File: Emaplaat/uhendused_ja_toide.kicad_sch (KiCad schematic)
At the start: 35 parts, among them IC4 TPS54429PWPR, IC5 FT232RNL-TUBE, J1 694108301002, J2 USB4216-03-A

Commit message: natuke parandusi
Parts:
- D7, D8, D9: Voltage (none) -> 3.3
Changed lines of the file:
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@@
 			)
 		)
+		(property "Voltage" "3.3"
+			(at 90.17 135.636 90)
+			(effects
+				(font
+					(size 1.27 1.27)
+				)
+			)
+		)
 		(pin "2"
 		)
@@
 	)
 	(symbol
-		(lib_name "CPDH3V3UP-HF_4")
-		(lib_id "CPDH3V3UP-HF:CPDH3V3UP-HF")
-		(at 91.44 115.57 270)
-		(unit 1)
-		(exclude_from_sim no)
-		(in_bom yes)
-		(on_board yes)
-		(dnp no)
-		(property "Reference" "D9"
-			(at 93.472 123.19 90)
-			(effects
-				(font
-					(size 1.27 1.27)
-				)
-				(justify left)
-			)
-		)
-		(property "Value" "CPDH3V3UP-HF"
-			(at 80.772 137.922 90)
-			(effects
-				(font
-					(size 1.27 1.27)
-				)
-				(justify left)
-			)
-		)
-		(property "Footprint" "Diode_SMD:D_SOD-523"
-			(at -2.21 125.73 0)
-			(effects
-				(font
-					(size 1.27 1.27)
-				)
-				(justify left bottom)
-				(hide yes)
-			)
-		)
-		(property "Datasheet" "https://datasheet.datasheetarchive.com/originals/distributors/Datasheets-DGA26/1842371.pdf"
-			(at -102.21 125.73 0)
-			(effects
-				(font
-					(size 1.27 1.27)
-				)
-				(justify left bottom)
-				(hide yes)
-			)
-		)
-		(property "Description" "ESD Suppressors / TVS Diodes 5.5V, 15Kv"
-			(at 105.156 115.316 0)
-			(effects
-				(font
-					(size 1.27 1.27)
-				)
-				(hide yes)
-			)
-		)
-		(property "Height" "0.77"
-			(at -302.21 125.73 0)
-			(effects
-				(font
-					(size 1.27 1.27)
-				)
-				(justify left bottom)
-				(hide yes)
-			)
-		)
-		(property "Mouser Part Number" "750-CPDH3V3UP-HF"
-			(at -402.21 125.73 0)
-			(effects
-				(font
-					(size 1.27 1.27)
-				)
-				(justify left bottom)
-				(hide yes)
-			)
-		)
-		(property "Mouser Price/Stock" "https://www.mouser.co.uk/ProductDetail/Comchip-Technology/CPDH3V3UP-HF?qs=XEIV%2Fho1H6em2DT135enQw%3D%3D"
-			(at -502.21 125.73 0)
-			(effects
-				(font
-					(size 1.27 1.27)
-				)
-				(justify left bottom)
-				(hide yes)
-			)
-		)
-		(property "Manufacturer_Name" "Comchip Technology"
-			(at -602.21 125.73 0)
-			(effects
-				(font
-					(size 1.27 1.27)
-				)
-				(justify left bottom)
-				(hide yes)
-			)
-		)
-		(property "Manufacturer_Part_Number" "CPDH3V3UP-HF"
-			(at -702.21 125.73 0)
-			(effects
-				(font
-					(size 1.27 1.27)
-				)
-				(justify left bottom)
-				(hide yes)
-			)
-		)
-		(pin "1"
-		)
-		(pin "2"
-		)
-		(instances
-			(project "Emaplaat"
-				(path "/489224c0-ace1-4530-aa61-a5d03adf1434/902edf26-f9ad-46ee-8658-d4b7491aa9c7"
-					(reference "D9")
-					(unit 1)
-				)
-			)
-		)
-	)
-	(symbol
 		(lib_id "Device:R")
 		(at 66.04 127 0)
@@
 	)
 	(symbol
+		(lib_name "CPDH3V3UP-HF_2")
+		(lib_id "CPDH3V3UP-HF:CPDH3V3UP-HF")
+		(at 91.44 115.57 270)
+		(unit 1)
+		(exclude_from_sim no)
+		(in_bom yes)
+		(on_board yes)
+		(dnp no)
+		(property "Reference" "D9"
+			(at 93.472 123.19 90)
+			(effects
+				(font
+					(size 1.27 1.27)
+				)
+				(justify left)
+			)
+		)
+		(property "Value" "CPDH3V3UP-HF"
+			(at 85.852 141.478 90)
+			(effects
+				(font
+					(size 1.27 1.27)
+				)
+				(justify left)
+			)
+		)
+		(property "Footprint" "Diode_SMD:D_SOD-523"
+			(at -2.21 125.73 0)
+			(effects
+				(font
+					(size 1.27 1.27)
+				)
+				(justify left bottom)
+				(hide yes)
+			)
+		)
+		(property "Datasheet" "https://datasheet.datasheetarchive.com/originals/distributors/Datasheets-DGA26/1842371.pdf"
+			(at -102.21 125.73 0)
+			(effects
+				(font
+					(size 1.27 1.27)
+				)
+				(justify left bottom)
+				(hide yes)
+			)
+		)
+		(property "Description" "ESD Suppressors / TVS Diodes 5.5V, 15Kv"
+			(at 105.156 115.316 0)
+			(effects
+				(font
+					(size 1.27 1.27)
+				)
+				(hide yes)
+			)
+		)
+		(property "Height" "0.77"
+			(at -302.21 125.73 0)
+			(effects
+				(font
+					(size 1.27 1.27)
+				)
+				(justify left bottom)
+				(hide yes)
+			)
+		)
+		(property "Mouser Part Number" "750-CPDH3V3UP-HF"
+			(at -402.21 125.73 0)
+			(effects
+				(font
+					(size 1.27 1.27)
+				)
+				(justify left bottom)
+				(hide yes)
+			)
+		)
+		(property "Mouser Price/Stock" "https://www.mouser.co.uk/ProductDetail/Comchip-Technology/CPDH3V3UP-HF?qs=XEIV%2Fho1H6em2DT135enQw%3D%3D"
+			(at -502.21 125.73 0)
+			(effects
+				(font
+					(size 1.27 1.27)
+				)
+				(justify left bottom)
+				(hide yes)
+			)
+		)
+		(property "Manufacturer_Name" "Comchip Technology"
+			(at -602.21 125.73 0)
+			(effects
+				(font
+					(size 1.27 1.27)
+				)
+				(justify left bottom)
+				(hide yes)
+			)
+		)
+		(property "Manufacturer_Part_Number" "CPDH3V3UP-HF"
+			(at -702.21 125.73 0)
+			(effects
+				(font
+					(size 1.27 1.27)
+				)
+				(justify left bottom)
+				(hide yes)
+			)
+		)
+		(property "Voltage" "3.3"
+			(at 99.568 143.256 90)
+			(effects
+				(font
+					(size 1.27 1.27)
+				)
+			)
+		)
+		(pin "2"
+		)
+		(pin "1"
+		)
+		(instances
+			(project "Emaplaat"
+				(path "/489224c0-ace1-4530-aa61-a5d03adf1434/902edf26-f9ad-46ee-8658-d4b7491aa9c7"
+					(reference "D9")
+					(unit 1)
+				)
+			)
+		)
+	)
+	(symbol
 		(lib_id "USB4216-03-A:USB4216-03-A")
 		(at 21.59 107.95 0)
@@
 		)
 		(property "Value" "CPDH3V3UP-HF"
-			(at 78.994 135.89 90)
+			(at 81.534 137.922 90)
 			(effects
 				(font
@@
 			)
 		)
+		(property "Voltage" "3.3"
+			(at 95.758 139.954 90)
+			(effects
+				(font
+					(size 1.27 1.27)
+				)
+			)
+		)

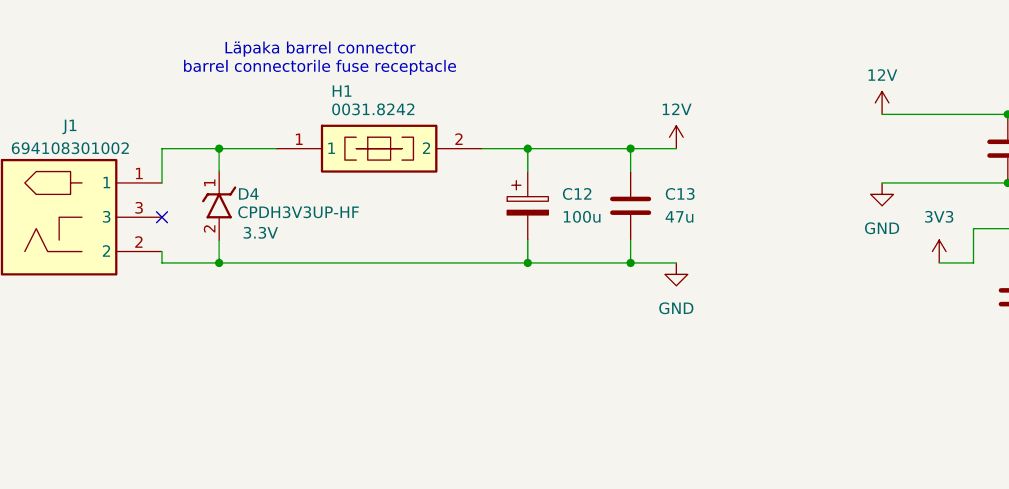
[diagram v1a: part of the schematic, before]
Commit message: Added electrolytic capacitors and 12V rated ESD diode
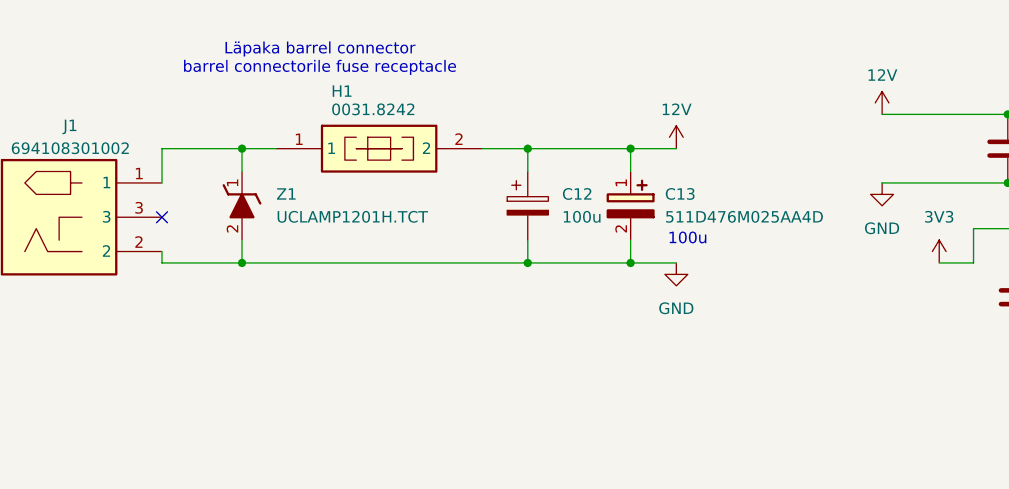
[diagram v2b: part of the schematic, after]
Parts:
- removed C13: 47u, Capacitor_SMD:C_0603_1608Metric_Pad1.08x0.95mm_HandSolder, symbol Device:C
- removed D4: CPDH3V3UP-HF, Diode_SMD:D_SOD-523, symbol CPDH3V3UP-HF:CPDH3V3UP-HF
- added C13: 511D476M025AA4D, 511D476M025AA4D, symbol 511D476M025AA4D:511D476M025AA4D
- added Z1: UCLAMP1201H.TCT, SODFL1608X70N, symbol UCLAMP1201H_TCT:UCLAMP1201H.TCT
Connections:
- net 12V: now also C13.1 (+)
- net AGND: now also C13.2 (-), Z1.2 (A)
- net at H1.1, J1.1: now also Z1.1 (K)
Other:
- note added: "100u"

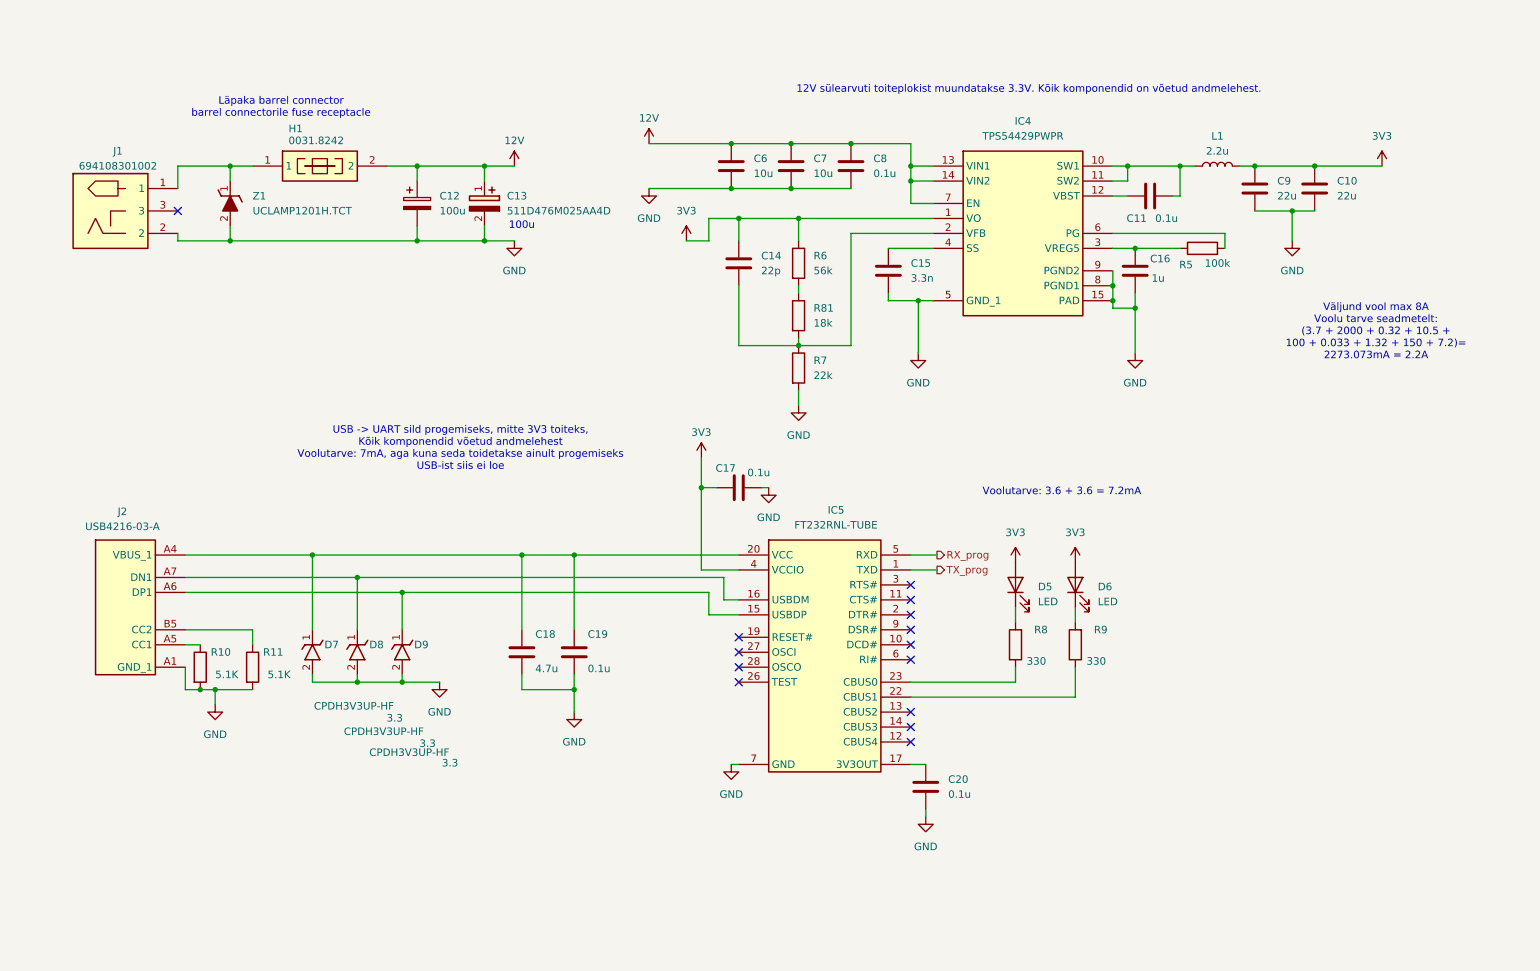
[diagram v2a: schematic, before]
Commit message: Lisasin kondensaatorid, mis on >3.3u footprindi ja sümbolid. Sammuti liigutasin ESP32 ja USC-C ühendused plaadi äärtele
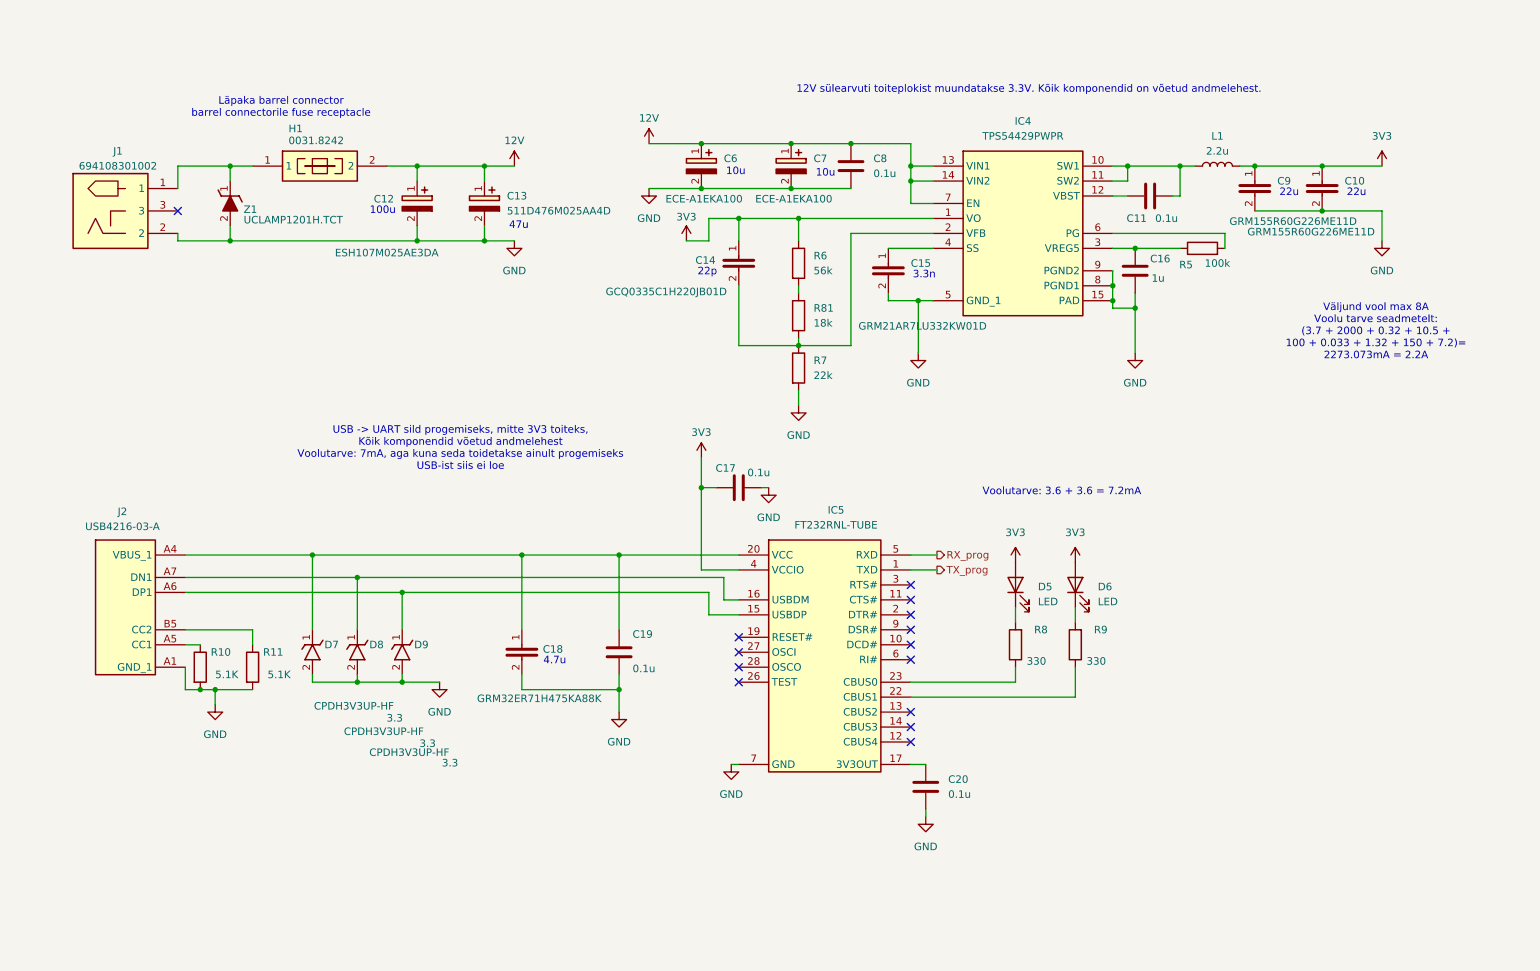
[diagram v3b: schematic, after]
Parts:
- removed C10, C9: 22u, Capacitor_SMD:C_0603_1608Metric_Pad1.08x0.95mm_HandSolder, symbol Device:C
- removed C12: 100u, Capacitor_SMD:C_0603_1608Metric_Pad1.08x0.95mm_HandSolder, symbol Device:C_Polarized
- removed C14: 22p, Capacitor_SMD:C_0603_1608Metric_Pad1.08x0.95mm_HandSolder, symbol Device:C
- removed C15: 3.3n, Capacitor_SMD:C_0603_1608Metric_Pad1.08x0.95mm_HandSolder, symbol Device:C
- removed C18: 4.7u, Capacitor_SMD:C_0603_1608Metric_Pad1.08x0.95mm_HandSolder, symbol Device:C
- removed C6, C7: 10u, Capacitor_SMD:C_0603_1608Metric_Pad1.08x0.95mm_HandSolder, symbol Device:C
- added C10, C9: GRM155R60G226ME11D, CAPC1005X70N, symbol GRM155R60G226ME11D:GRM155R60G226ME11D
- added C12: ESH107M025AE3DA, CAPPRD250W50D630H1250, symbol ESH107M025AE3DA:ESH107M025AE3DA
- added C14: GCQ0335C1H220JB01D, CAPC0603X33N, symbol GCQ0335C1H220JB01D:GCQ0335C1H220JB01D
- added C15: GRM21AR7LU332KW01D, CAPC2012X130N, symbol GRM21AR7LU332KW01D:GRM21AR7LU332KW01D
- added C18: GRM32ER71H475KA88K, CAPC3225X270N, symbol GRM32ER71H475KA88K:GRM32ER71H475KA88K
- added C6, C7: ECE-A1EKA100, CAPPRD150W50D400H800, symbol ECE-A1EKN100:ECE-A1EKA100
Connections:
- net 12V: now also C12.1 (+), C6.1 (+), C7.1 (+)
- net 3V3: now also C10.1, C14.1, C9.1
- net AGND: now also C10.2, C12.2 (-), C15.2, C18.2, C6.2 (-), C7.2 (-), C9.2
- net at IC4.2 (VFB), R7.1, R81.2: now also C14.2
- net at IC4.4 (SS): now also C15.1
- net at C19.1, D7.1 (K), IC5.20 (VCC)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: now also C18.1
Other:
- note added: "10u"
- note added: "22p"
- note added: "22u"
- note added: "3.3n"
- note added: "4.7u"
- note added: "47u"
- moved on the sheet: C19

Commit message: v1.1 kuid veel pooleli
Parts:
- removed L1: 2.2u, Inductor_SMD:L_0805_2012Metric_Pad1.05x1.20mm_HandSolder, symbol Device:L
- added L1: SRP2512TMA-2R2M, SRP2512TMA2R2M, symbol SRP2512TMA-2R2M:SRP2512TMA-2R2M
- C8: footprint Capacitor_SMD:C_0603_1608Metric_Pad1.08x0.95mm_HandSolder -> Capacitor_SMD:C_0805_2012Metric_Pad1.18x1.45mm_HandSolder
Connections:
- net 12V: now also Z1.1 (K)
- net 3V3: now also L1.2
- net at C11.2, IC4.10 (SW1), IC4.11 (SW2): now also L1.1
- net at H1.1, J1.1: no longer Z1.1 (K)
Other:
- note added: "Induktorile langeb: peak-to-peak ripple current=1.55A;peak current=2.98A;RMS current=2.25A Induktor kannatab: peak current=3.1A; saturation current=3.4A"
- moved on the sheet: C10, C9, H1, Z1

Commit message: v1.2 peaaegu valmis, aint 5V esd dioodid vaja lisada
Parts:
- removed D7, D8, D9: CPDH3V3UP-HF, Diode_SMD:D_SOD-523, symbol CPDH3V3UP-HF:CPDH3V3UP-HF
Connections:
- net SW_DC_DC: now reaches C11.2, IC4.10 (SW1), IC4.11 (SW2), L1.1
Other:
- note added: "Siia vaja 5V working voltage ESD dioodid panna"

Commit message: v1.5 valmis, juhendajad andsid rohelise tule
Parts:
- removed C10, C9: GRM155R60G226ME11D, CAPC1005X70N, symbol GRM155R60G226ME11D:GRM155R60G226ME11D
- removed C14: GCQ0335C1H220JB01D, CAPC0603X33N, symbol GCQ0335C1H220JB01D:GCQ0335C1H220JB01D
- added C10, C9: 22u, Capacitor_SMD:C_1206_3216Metric_Pad1.33x1.80mm_HandSolder, symbol Device:C
- added C14: 22p, Capacitor_SMD:C_0603_1608Metric_Pad1.08x0.95mm_HandSolder, symbol Device:C
- added Z2, Z3, Z4: ESD5Z5V0, Diode_SMD:D_SOD-523, symbol UCLAMP1201H_TCT:UCLAMP1201H.TCT
- C8: footprint Capacitor_SMD:C_0805_2012Metric_Pad1.18x1.45mm_HandSolder -> Capacitor_SMD:C_0603_1608Metric_Pad1.08x0.95mm_HandSolder
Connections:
- net 3V3: now also C10.1, C14.1, C9.1
- net AGND: now also C10.2, C9.2, Z2.2 (A), Z3.2 (A), Z4.2 (A)
- net at IC4.2 (VFB), R7.1, R81.2: now also C14.2
- net at C18.1, C19.1, IC5.20 (VCC)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: now also Z2.1 (K)
- net at IC5.15 (USBDP), J2.A6 (DP1), J2.B6 (DP2): now also Z4.1 (K)
- net at IC5.16 (USBDM), J2.A7 (DN1), J2.B7 (DN2): now also Z3.1 (K)
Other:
- note removed: "22p"
- note removed: "22u"

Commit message: uus BOM ja asendasin 0.1uF kondeka
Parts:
- C14: Product (none) -> C0603C220M5HACTU; Store link (none) -> https://www.mouser.ee/ProductDetail/KEMET/C0603C220M5HACTU?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
- C8: product (none) -> CL10B104KA8NNNL; store link (none) -> https://www.mouser.ee/ProductDetail/Samsung-Electro-Mechani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
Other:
- note added: "C6, C7, C8, C12, C13 on kõik 25VDC rated"
- moved on the sheet: C10, C11, C12, C13, C14, C15, C16, C17, C18, C19, C20, C6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

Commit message: v3.0 Abeltoni tagaside implement
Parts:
- added TP29, TP30: TestPoint, TestPoint:TestPoint_Pad_D1.0mm, symbol Connector:TestPoint
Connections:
- net 12V: now also TP30.1
- net 3V3: now also TP29.1
